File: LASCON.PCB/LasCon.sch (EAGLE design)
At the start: 11 parts

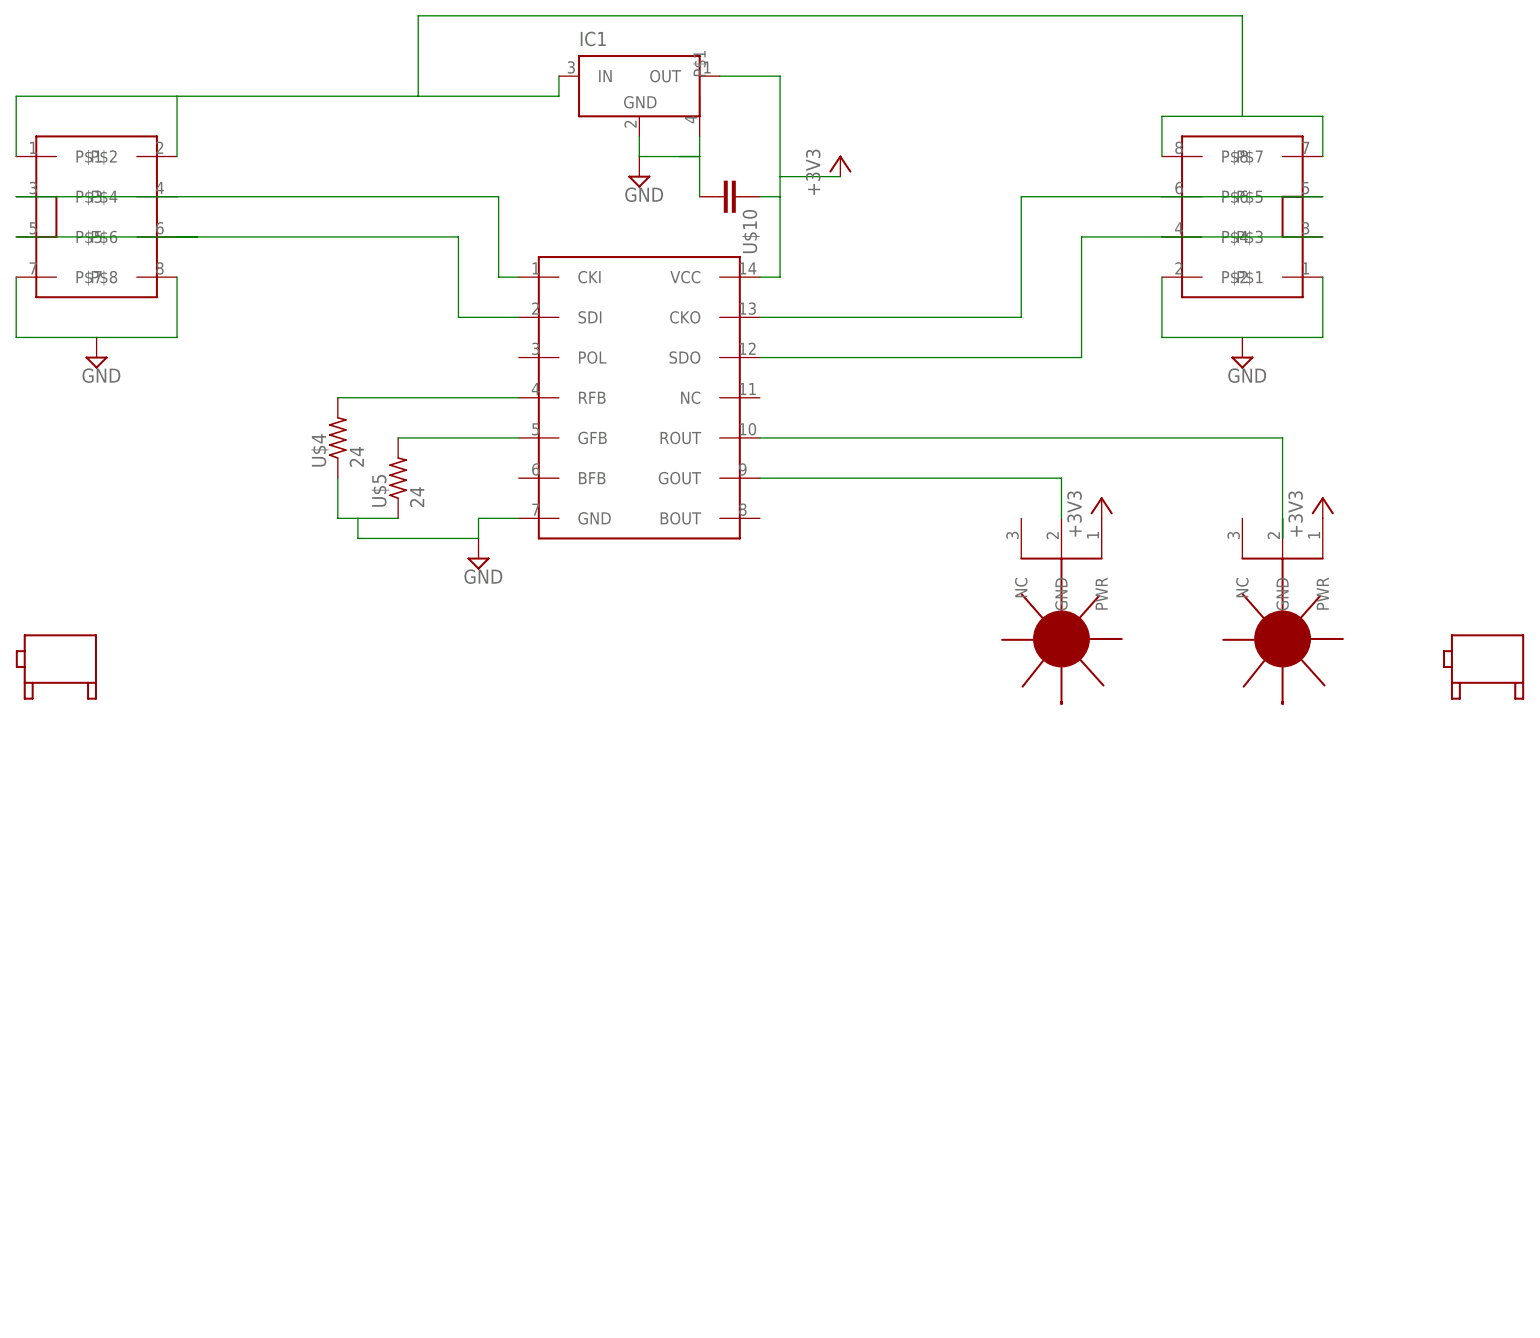
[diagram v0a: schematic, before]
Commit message: Added LED & 3rd laser
Added LED and 3rd laser, with pingpong ball outline
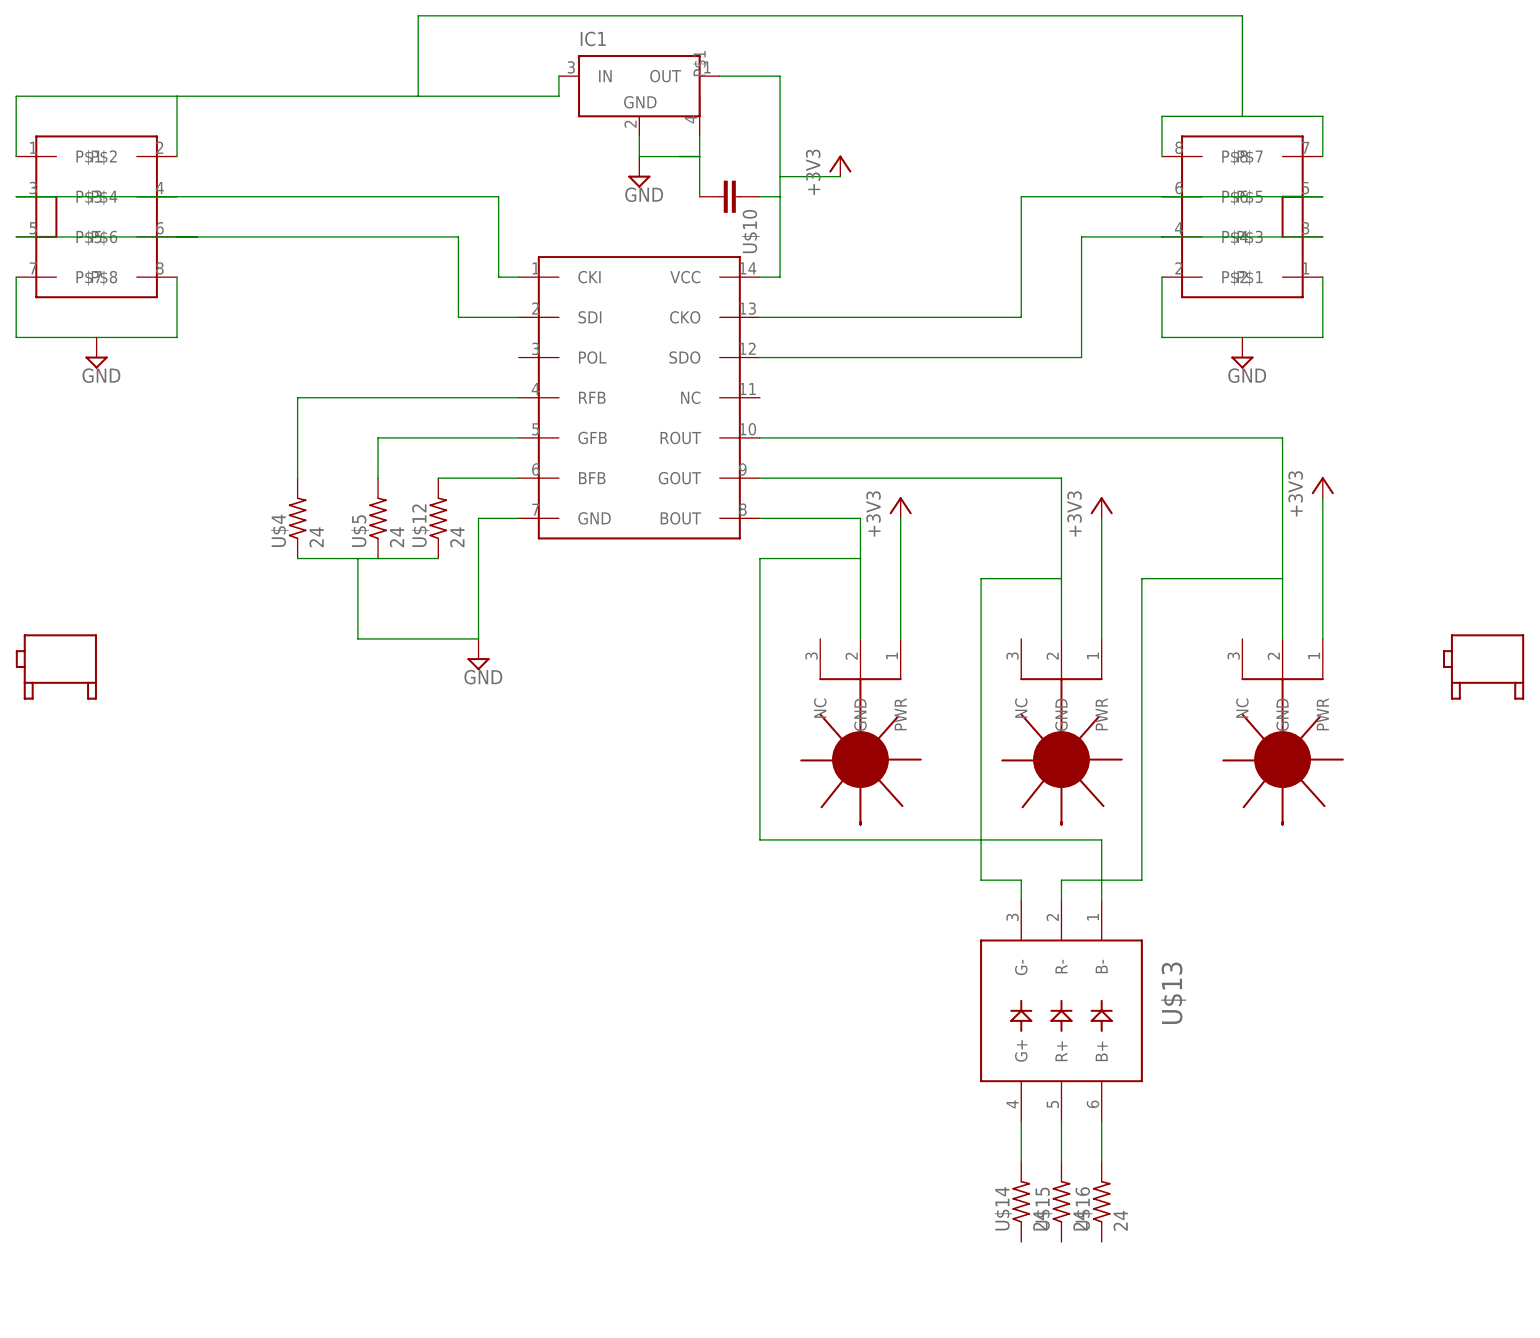
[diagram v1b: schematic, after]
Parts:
- added U$11: LASER, GW-devices:LASER
- added U$12, U$14, U$15, U$16: 24, GW-devices:RF-R0805
- added U$13: LED5060A, GW-devices:LED5060A
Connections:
- new net N$11: U$12.2, U$3.BFB
- new net N$12: U$13.G+, U$14.2
- new net N$13: U$13.R+, U$15.2
- new net N$14: U$13.B+, U$16.2
- new net N$4: U$11.GND, U$13.B-, U$3.BOUT
- net +3V3: now also U$11.PWR
- net GND: now also U$12.1
- net N$2: now also U$13.G-
- net N$3: now also U$13.R-
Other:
- moved on the sheet: U$4, U$5
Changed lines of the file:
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@@
 <part name="U$9" library="GW-devices" deviceset="90DEGMNT" device=""/>
 <part name="U$10" library="GW-devices" deviceset="RF-C" device="0805"/>
+<part name="U$11" library="GW-devices" deviceset="LASER" device=""/>
+<part name="+3V4" library="supply1" deviceset="+3V3" device=""/>
+<part name="U$12" library="GW-devices" deviceset="RF-R" device="0805" value="24"/>
+<part name="U$13" library="GW-devices" deviceset="LED5060" device="A"/>
+<part name="U$14" library="GW-devices" deviceset="RF-R" device="0805" value="24"/>
+<part name="U$15" library="GW-devices" deviceset="RF-R" device="0805" value="24"/>
+<part name="U$16" library="GW-devices" deviceset="RF-R" device="0805" value="24"/>
 </parts>
 <sheets>
@@
 <instance part="SUPPLY2" gate="GND" x="-55.88" y="-15.24"/>
 <instance part="SUPPLY3" gate="GND" x="88.9" y="-15.24"/>
-<instance part="SUPPLY4" gate="GND" x="-7.62" y="-40.64"/>
+<instance part="SUPPLY4" gate="GND" x="-7.62" y="-53.34"/>
 <instance part="IC1" gate="G$1" x="12.7" y="17.78"/>
-<instance part="U$4" gate="G$1" x="-25.4" y="-25.4" rot="R90"/>
-<instance part="U$5" gate="G$1" x="-17.78" y="-30.48" rot="R90"/>
-<instance part="U$6" gate="G$1" x="66.04" y="-43.18" rot="R270"/>
-<instance part="U$7" gate="G$1" x="93.98" y="-43.18" rot="R270"/>
+<instance part="U$4" gate="G$1" x="-30.48" y="-35.56" rot="R90"/>
+<instance part="U$5" gate="G$1" x="-20.32" y="-35.56" rot="R90"/>
+<instance part="U$6" gate="G$1" x="66.04" y="-58.42" rot="R270"/>
+<instance part="U$7" gate="G$1" x="93.98" y="-58.42" rot="R270"/>
 <instance part="+3V1" gate="G$1" x="38.1" y="10.16"/>
 <instance part="+3V2" gate="G$1" x="71.12" y="-33.02"/>
-<instance part="+3V3" gate="G$1" x="99.06" y="-33.02"/>
+<instance part="+3V3" gate="G$1" x="99.06" y="-30.48"/>
 <instance part="U$8" gate="G$1" x="-60.96" y="-53.34"/>
 <instance part="U$9" gate="G$1" x="119.38" y="-53.34"/>
 <instance part="U$10" gate="G$1" x="25.4" y="5.08" rot="R270"/>
+<instance part="U$11" gate="G$1" x="40.64" y="-58.42" rot="R270"/>
+<instance part="+3V4" gate="G$1" x="45.72" y="-33.02"/>
+<instance part="U$12" gate="G$1" x="-12.7" y="-35.56" rot="R90"/>
+<instance part="U$13" gate="G$1" x="66.04" y="-96.52" rot="R270"/>
+<instance part="U$14" gate="G$1" x="60.96" y="-121.92" rot="R90"/>
+<instance part="U$15" gate="G$1" x="66.04" y="-121.92" rot="R90"/>
+<instance part="U$16" gate="G$1" x="71.12" y="-121.92" rot="R90"/>
 </instances>
 <busses>
@@
 <pinref part="SUPPLY4" gate="GND" pin="GND"/>
 <wire x1="-2.54" y1="-35.56" x2="-7.62" y2="-35.56" width="0.1524" layer="91"/>
-<wire x1="-7.62" y1="-35.56" x2="-7.62" y2="-38.1" width="0.1524" layer="91"/>
+<wire x1="-7.62" y1="-35.56" x2="-7.62" y2="-50.8" width="0.1524" layer="91"/>
 <pinref part="U$4" gate="G$1" pin="1"/>
-<wire x1="-25.4" y1="-30.48" x2="-25.4" y2="-35.56" width="0.1524" layer="91"/>
+<wire x1="-30.48" y1="-40.64" x2="-25.4" y2="-40.64" width="0.1524" layer="91"/>
 <pinref part="U$5" gate="G$1" pin="1"/>
-<wire x1="-25.4" y1="-35.56" x2="-22.86" y2="-35.56" width="0.1524" layer="91"/>
-<wire x1="-22.86" y1="-35.56" x2="-17.78" y2="-35.56" width="0.1524" layer="91"/>
-<wire x1="-7.62" y1="-38.1" x2="-22.86" y2="-38.1" width="0.1524" layer="91"/>
-<wire x1="-22.86" y1="-38.1" x2="-22.86" y2="-35.56" width="0.1524" layer="91"/>
+<wire x1="-25.4" y1="-40.64" x2="-22.86" y2="-40.64" width="0.1524" layer="91"/>
+<wire x1="-22.86" y1="-40.64" x2="-20.32" y2="-40.64" width="0.1524" layer="91"/>
+<wire x1="-7.62" y1="-50.8" x2="-22.86" y2="-50.8" width="0.1524" layer="91"/>
+<wire x1="-22.86" y1="-50.8" x2="-22.86" y2="-40.64" width="0.1524" layer="91"/>
+<pinref part="U$12" gate="G$1" pin="1"/>
+<wire x1="-20.32" y1="-40.64" x2="-12.7" y2="-40.64" width="0.1524" layer="91"/>
 </segment>
 <segment>
@@
 <pinref part="U$4" gate="G$1" pin="2"/>
 <pinref part="U$3" gate="G$1" pin="RFB"/>
-<wire x1="-25.4" y1="-20.32" x2="-2.54" y2="-20.32" width="0.1524" layer="91"/>
+<wire x1="-30.48" y1="-30.48" x2="-30.48" y2="-20.32" width="0.1524" layer="91"/>
+<wire x1="-30.48" y1="-20.32" x2="-2.54" y2="-20.32" width="0.1524" layer="91"/>
 </segment>
 </net>
@@
 <pinref part="U$3" gate="G$1" pin="GFB"/>
 <pinref part="U$5" gate="G$1" pin="2"/>
-<wire x1="-2.54" y1="-25.4" x2="-17.78" y2="-25.4" width="0.1524" layer="91"/>
+<wire x1="-2.54" y1="-25.4" x2="-20.32" y2="-25.4" width="0.1524" layer="91"/>
+<wire x1="-20.32" y1="-25.4" x2="-20.32" y2="-30.48" width="0.1524" layer="91"/>
 </segment>
 </net>
@@
 <segment>
 <pinref part="U$7" gate="G$1" pin="GND"/>
-<wire x1="93.98" y1="-35.56" x2="93.98" y2="-38.1" width="0.1524" layer="91"/>
+<wire x1="93.98" y1="-50.8" x2="93.98" y2="-43.18" width="0.1524" layer="91"/>
 <pinref part="U$3" gate="G$1" pin="ROUT"/>
+<wire x1="93.98" y1="-43.18" x2="93.98" y2="-38.1" width="0.1524" layer="91"/>
 <wire x1="27.94" y1="-25.4" x2="93.98" y2="-25.4" width="0.1524" layer="91"/>
 <wire x1="93.98" y1="-25.4" x2="93.98" y2="-38.1" width="0.1524" layer="91"/>
+<wire x1="93.98" y1="-43.18" x2="76.2" y2="-43.18" width="0.1524" layer="91"/>
+<wire x1="76.2" y1="-43.18" x2="76.2" y2="-81.28" width="0.1524" layer="91"/>
+<pinref part="U$13" gate="G$1" pin="R-"/>
+<wire x1="76.2" y1="-81.28" x2="66.04" y2="-81.28" width="0.1524" layer="91"/>
+<wire x1="66.04" y1="-81.28" x2="66.04" y2="-83.82" width="0.1524" layer="91"/>
 </segment>
 </net>
@@
 <pinref part="U$6" gate="G$1" pin="PWR"/>
 <pinref part="+3V2" gate="G$1" pin="+3V3"/>
+<wire x1="71.12" y1="-50.8" x2="71.12" y2="-35.56" width="0.1524" layer="91"/>
 </segment>
 <segment>
 <pinref part="U$7" gate="G$1" pin="PWR"/>
 <pinref part="+3V3" gate="G$1" pin="+3V3"/>
+<wire x1="99.06" y1="-33.02" x2="99.06" y2="-50.8" width="0.1524" layer="91"/>
 </segment>
 <segment>
@@
 <wire x1="27.94" y1="5.08" x2="30.48" y2="5.08" width="0.1524" layer="91"/>
 </segment>
+<segment>
+<pinref part="+3V4" gate="G$1" pin="+3V3"/>
+<pinref part="U$11" gate="G$1" pin="PWR"/>
+<wire x1="45.72" y1="-35.56" x2="45.72" y2="-50.8" width="0.1524" layer="91"/>
+</segment>
 </net>
 <net name="N$2" class="0">
 <segment>
 <pinref part="U$6" gate="G$1" pin="GND"/>
-<wire x1="66.04" y1="-35.56" x2="66.04" y2="-30.48" width="0.1524" layer="91"/>
+<wire x1="66.04" y1="-50.8" x2="66.04" y2="-43.18" width="0.1524" layer="91"/>
 <pinref part="U$3" gate="G$1" pin="GOUT"/>
+<wire x1="66.04" y1="-43.18" x2="66.04" y2="-30.48" width="0.1524" layer="91"/>
 <wire x1="66.04" y1="-30.48" x2="27.94" y2="-30.48" width="0.1524" layer="91"/>
-</segment>
-</net>
+<wire x1="66.04" y1="-43.18" x2="55.88" y2="-43.18" width="0.1524" layer="91"/>
+<wire x1="55.88" y1="-43.18" x2="55.88" y2="-81.28" width="0.1524" layer="91"/>
+<pinref part="U$13" gate="G$1" pin="G-"/>
+<wire x1="55.88" y1="-81.28" x2="60.96" y2="-81.28" width="0.1524" layer="91"/>
+<wire x1="60.96" y1="-81.28" x2="60.96" y2="-83.82" width="0.1524" layer="91"/>
+</segment>
+</net>
+<net name="N$4" class="0">
+<segment>
+<pinref part="U$3" gate="G$1" pin="BOUT"/>
+<pinref part="U$11" gate="G$1" pin="GND"/>
+<wire x1="27.94" y1="-35.56" x2="40.64" y2="-35.56" width="0.1524" layer="91"/>
+<wire x1="40.64" y1="-35.56" x2="40.64" y2="-40.64" width="0.1524" layer="91"/>
+<wire x1="40.64" y1="-40.64" x2="40.64" y2="-50.8" width="0.1524" layer="91"/>
+<wire x1="40.64" y1="-40.64" x2="27.94" y2="-40.64" width="0.1524" layer="91"/>
+<wire x1="27.94" y1="-40.64" x2="27.94" y2="-76.2" width="0.1524" layer="91"/>
+<pinref part="U$13" gate="G$1" pin="B-"/>
+<wire x1="27.94" y1="-76.2" x2="71.12" y2="-76.2" width="0.1524" layer="91"/>
+<wire x1="71.12" y1="-76.2" x2="71.12" y2="-83.82" width="0.1524" layer="91"/>
+</segment>
+</net>
+<net name="N$11" class="0">
+<segment>
+<pinref part="U$3" gate="G$1" pin="BFB"/>
+<pinref part="U$12" gate="G$1" pin="2"/>
+<wire x1="-2.54" y1="-30.48" x2="-12.7" y2="-30.48" width="0.1524" layer="91"/>
+</segment>
+</net>
+<net name="N$12" class="0">
+<segment>
+<pinref part="U$13" gate="G$1" pin="G+"/>
+<pinref part="U$14" gate="G$1" pin="2"/>
+<wire x1="60.96" y1="-111.76" x2="60.96" y2="-116.84" width="0.1524" layer="91"/>
+</segment>
+</net>
+<net name="N$13" class="0">
+<segment>
+<pinref part="U$13" gate="G$1" pin="R+"/>
+<pinref part="U$15" gate="G$1" pin="2"/>
+<wire x1="66.04" y1="-111.76" x2="66.04" y2="-116.84" width="0.1524" layer="91"/>
+</segment>
+</net>
+<net name="N$14" class="0">
+<segment>
+<pinref part="U$13" gate="G$1" pin="B+"/>
+<pinref part="U$16" gate="G$1" pin="2"/>
+<wire x1="71.12" y1="-111.76" x2="71.12" y2="-116.84" width="0.1524" layer="91"/>
+</segment>
+</net>
